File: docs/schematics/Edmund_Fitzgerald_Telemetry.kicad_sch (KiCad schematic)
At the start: 0 parts

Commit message: Save stable KiCAD schematic base with verified ESP32 pinout
- Verified all GPIO mappings against boat_telemetry.ino
- Established correct ESP32-WROOM-32 symbol and wiring base
- Includes labels for Audio, RC, Power, and Lighting sections
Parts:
- added U1: ESP32_Control, symbol MCU_Espressif:ESP32-WROOM-32
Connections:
- new net 3V3: U1.1 (3V3)
- new net BAT_SENSE: U1.5 (IO34)
- new net DFP_RX: U1.11 (IO27)
- new net DFP_TX: U1.10 (IO26)
- new net FLOOD_GATE: U1.33 (IO21)
- new net FLOOD_LED: U1.26 (IO4)
- new net GND: U1.15 (GND)
- new net I2S_BCLK: U1.9 (IO25)
- new net I2S_DIN: U1.37 (IO23)
- new net I2S_LRC: U1.36 (IO22)
- new net RUN_GATE: U1.25 (IO16)
- new net RUN_LED: U1.24 (IO2)
- new net SERVO_RC: U1.31 (IO19)
- new net THROTTLE_RC: U1.30 (IO18)
- new net WATER_SENSOR: U1.7 (IO32)
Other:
- removed sheet ?
- note added: "100k/47k Resistor Divider for 8.4V sensing"
- note added: "AUDIO SECTION"
- note added: "I2S: BCLK, LRC, DIN -> MAX98357A"
- note added: "IO16/IO21 drive N-Channel MOSFET Gates"
- note added: "LIGHTING SECTION"
- note added: "POWER SENSE"
- note added: "Throttle (IO18), Servo (IO19) 5V PWM"
- note added: "UART: TX, RX -> DFPlayer Pro"
- note removed: "AUDIO SYSTEM"
- note removed: "Battery ADC on GPIO 34 with voltage divider"
- note removed: "Built-in WiFi 2.4GHz for telemetry and OTA updates"
- note removed: "CAMERA SYSTEM"
- note removed: "CONNECTIVITY"
- note removed: "Connected to MAX98357A Class-D Amplifier"
- note removed: "Core 0 handles WiFi and HTTP Server"
- note removed: "Core 1 runs Audio Engine with real-time I2S"
- note removed: "DFPlayer Pro on GPIO 27 RX, 26 TX at 115200 baud"
- note removed: "GPIO 18 captures Throttle PWM signal"
- note removed: "GPIO 19 captures Servo Rudder PWM signal"
- note removed: "GPIO 2 and GPIO 16 control running lights"
- note removed: "GPIO 4 and GPIO 21 control flood lights"
- note removed: "I2S output on GPIO 25 (BCLK), 22 (LRC), 23 (DIN)"
- note removed: "LED CONTROL"
- note removed: "Main Controller: ESP32 Dual-Core"
- note removed: "POWER: 8.4V LiPo battery"
- note removed: "SENSORS"
- note removed: "Separate ESP32-CAM with AI-Thinker OV2640"
- note removed: "Water intrusion sensor on GPIO 32 with pullup"
- title: Edmund Fitzgerald Telemetry System -> Edmund Fitzgerald - Platform Telemetry
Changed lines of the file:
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@@
 (kicad_sch (version 20230121) (generator eeschema)
  (paper "A3")
- (title_block
-  (title "Edmund Fitzgerald Telemetry System")
-  (date "2026-01-31")
-  (rev "1.0")
-  (company "Project Edmund Fitzgerald")
- )
- (sheet (at 0 0) (size 297 210))
- (text "POWER: 8.4V LiPo battery"
-  (at 25 50 0)
-  (effects (font (size 2 2) (thickness 0.15)) (justify left))
- )
- (text "Main Controller: ESP32 Dual-Core"
-  (at 25 80 0)
-  (effects (font (size 1.5 1.5) (thickness 0.12)) (justify left))
- )
- (text "Core 0 handles WiFi and HTTP Server"
-  (at 25 95 0)
-  (effects (font (size 1 1) (thickness 0.1)) (justify left))
- )
- (text "Core 1 runs Audio Engine with real-time I2S"
-  (at 25 110 0)
-  (effects (font (size 1 1) (thickness 0.1)) (justify left))
- )
- (text "AUDIO SYSTEM"
-  (at 25 140 0)
-  (effects (font (size 1.5 1.5) (thickness 0.12)) (justify left))
- )
- (text "I2S output on GPIO 25 (BCLK), 22 (LRC), 23 (DIN)"
-  (at 25 155 0)
-  (effects (font (size 1 1) (thickness 0.1)) (justify left))
- )
- (text "Connected to MAX98357A Class-D Amplifier"
-  (at 25 170 0)
-  (effects (font (size 1 1) (thickness 0.1)) (justify left))
- )
- (text "DFPlayer Pro on GPIO 27 RX, 26 TX at 115200 baud"
-  (at 25 185 0)
-  (effects (font (size 1 1) (thickness 0.1)) (justify left))
- )
- (text "SENSORS"
-  (at 25 215 0)
-  (effects (font (size 1.5 1.5) (thickness 0.12)) (justify left))
- )
- (text "Battery ADC on GPIO 34 with voltage divider"
-  (at 25 230 0)
-  (effects (font (size 1 1) (thickness 0.1)) (justify left))
- )
- (text "Water intrusion sensor on GPIO 32 with pullup"
-  (at 25 245 0)
-  (effects (font (size 1 1) (thickness 0.1)) (justify left))
- )
- (text "LED CONTROL"
-  (at 25 275 0)
-  (effects (font (size 1.5 1.5) (thickness 0.12)) (justify left))
- )
- (text "GPIO 2 and GPIO 16 control running lights"
-  (at 25 290 0)
-  (effects (font (size 1 1) (thickness 0.1)) (justify left))
- )
- (text "GPIO 4 and GPIO 21 control flood lights"
-  (at 25 305 0)
-  (effects (font (size 1 1) (thickness 0.1)) (justify left))
- )
- (text "RC RECEIVER"
-  (at 25 335 0)
-  (effects (font (size 1.5 1.5) (thickness 0.12)) (justify left))
- )
- (text "GPIO 18 captures Throttle PWM signal"
-  (at 25 350 0)
-  (effects (font (size 1 1) (thickness 0.1)) (justify left))
- )
- (text "GPIO 19 captures Servo Rudder PWM signal"
-  (at 25 365 0)
-  (effects (font (size 1 1) (thickness 0.1)) (justify left))
- )
- (text "CAMERA SYSTEM"
-  (at 25 395 0)
-  (effects (font (size 1.5 1.5) (thickness 0.12)) (justify left))
- )
- (text "Separate ESP32-CAM with AI-Thinker OV2640"
-  (at 25 410 0)
-  (effects (font (size 1 1) (thickness 0.1)) (justify left))
- )
- (text "CONNECTIVITY"
-  (at 25 440 0)
-  (effects (font (size 1.5 1.5) (thickness 0.12)) (justify left))
- )
- (text "Built-in WiFi 2.4GHz for telemetry and OTA updates"
-  (at 25 455 0)
-  (effects (font (size 1 1) (thickness 0.1)) (justify left))
- )
+ (title_block (title "Edmund Fitzgerald - Platform Telemetry") (company "Project Edmund Fitzgerald") (rev "1.1") (date "2026-01-31"))
+ (symbol (lib_id "MCU_Espressif:ESP32-WROOM-32") (at 150 100 0) (unit 1) (in_bom yes) (on_board yes) (fields_autoplaced yes)
+  (property "Reference" "U1" (at 150 75 0)) (property "Value" "ESP32_Control" (at 150 125 0)))
+  (wire (pts (xy 134.76 84.76) (xy 120 84.76)) (stroke (width 0) (type solid)))
+  (label "3V3" (at 120 84.76 0) (effects (font (size 1.27 1.27)) (justify left bottom)))
+  (wire (pts (xy 134.76 94.92) (xy 120 94.92)) (stroke (width 0) (type solid)))
+  (label "BAT_SENSE" (at 120 94.92 0) (effects (font (size 1.27 1.27)) (justify left bottom)))
+  (wire (pts (xy 134.76 100) (xy 120 100)) (stroke (width 0) (type solid)))
+  (label "WATER_SENSOR" (at 120 100 0) (effects (font (size 1.27 1.27)) (justify left bottom)))
+  (wire (pts (xy 134.76 105.08) (xy 120 105.08)) (stroke (width 0) (type solid)))
+  (label "I2S_BCLK" (at 120 105.08 0) (effects (font (size 1.27 1.27)) (justify left bottom)))
+  (wire (pts (xy 134.76 107.62) (xy 120 107.62)) (stroke (width 0) (type solid)))
+  (label "DFP_TX" (at 120 107.62 0) (effects (font (size 1.27 1.27)) (justify left bottom)))
+  (wire (pts (xy 134.76 110.16) (xy 120 110.16)) (stroke (width 0) (type solid)))
+  (label "DFP_RX" (at 120 110.16 0) (effects (font (size 1.27 1.27)) (justify left bottom)))
+  (wire (pts (xy 150 120.32) (xy 150 130)) (stroke (width 0) (type solid)))
+  (label "GND" (at 150 130 90) (effects (font (size 1.27 1.27)) (justify left bottom)))
+  (wire (pts (xy 165.24 115.24) (xy 180 115.24)) (stroke (width 0) (type solid)))
+  (label "I2S_DIN" (at 180 115.24 0) (effects (font (size 1.27 1.27)) (justify left bottom)))
+  (wire (pts (xy 165.24 112.7) (xy 180 112.7)) (stroke (width 0) (type solid)))
+  (label "I2S_LRC" (at 180 112.7 0) (effects (font (size 1.27 1.27)) (justify left bottom)))
+  (wire (pts (xy 165.24 110.16) (xy 180 110.16)) (stroke (width 0) (type solid)))
+  (label "FLOOD_GATE" (at 180 110.16 0) (effects (font (size 1.27 1.27)) (justify left bottom)))
+  (wire (pts (xy 165.24 107.62) (xy 180 107.62)) (stroke (width 0) (type solid)))
+  (label "SERVO_RC" (at 180 107.62 0) (effects (font (size 1.27 1.27)) (justify left bottom)))
+  (wire (pts (xy 165.24 105.08) (xy 180 105.08)) (stroke (width 0) (type solid)))
+  (label "THROTTLE_RC" (at 180 105.08 0) (effects (font (size 1.27 1.27)) (justify left bottom)))
+  (wire (pts (xy 165.24 102.54) (xy 180 102.54)) (stroke (width 0) (type solid)))
+  (label "FLOOD_LED" (at 180 102.54 0) (effects (font (size 1.27 1.27)) (justify left bottom)))
+  (wire (pts (xy 165.24 100) (xy 180 100)) (stroke (width 0) (type solid)))
+  (label "RUN_LED" (at 180 100 0) (effects (font (size 1.27 1.27)) (justify left bottom)))
+  (wire (pts (xy 165.24 97.46) (xy 180 97.46)) (stroke (width 0) (type solid)))
+  (label "RUN_GATE" (at 180 97.46 0) (effects (font (size 1.27 1.27)) (justify left bottom)))
+ (text "AUDIO SECTION" (at 210 110 0) (effects (font (size 2 2)) (justify left)))
+ (text "I2S: BCLK, LRC, DIN -> MAX98357A" (at 210 118 0) (effects (font (size 1 1)) (justify left)))
+ (text "UART: TX, RX -> DFPlayer Pro" (at 210 123 0) (effects (font (size 1 1)) (justify left)))
+ (text "LIGHTING SECTION" (at 210 90 0) (effects (font (size 2 2)) (justify left)))
+ (text "IO16/IO21 drive N-Channel MOSFET Gates" (at 210 98 0) (effects (font (size 1 1)) (justify left)))
+ (text "RC RECEIVER" (at 210 140 0) (effects (font (size 2 2)) (justify left)))
+ (text "Throttle (IO18), Servo (IO19) 5V PWM" (at 210 148 0) (effects (font (size 1 1)) (justify left)))
+ (text "POWER SENSE" (at 80 90 0) (effects (font (size 2 2)) (justify right)))
+ (text "100k/47k Resistor Divider for 8.4V sensing" (at 80 98 0) (effects (font (size 1 1)) (justify right)))
 )

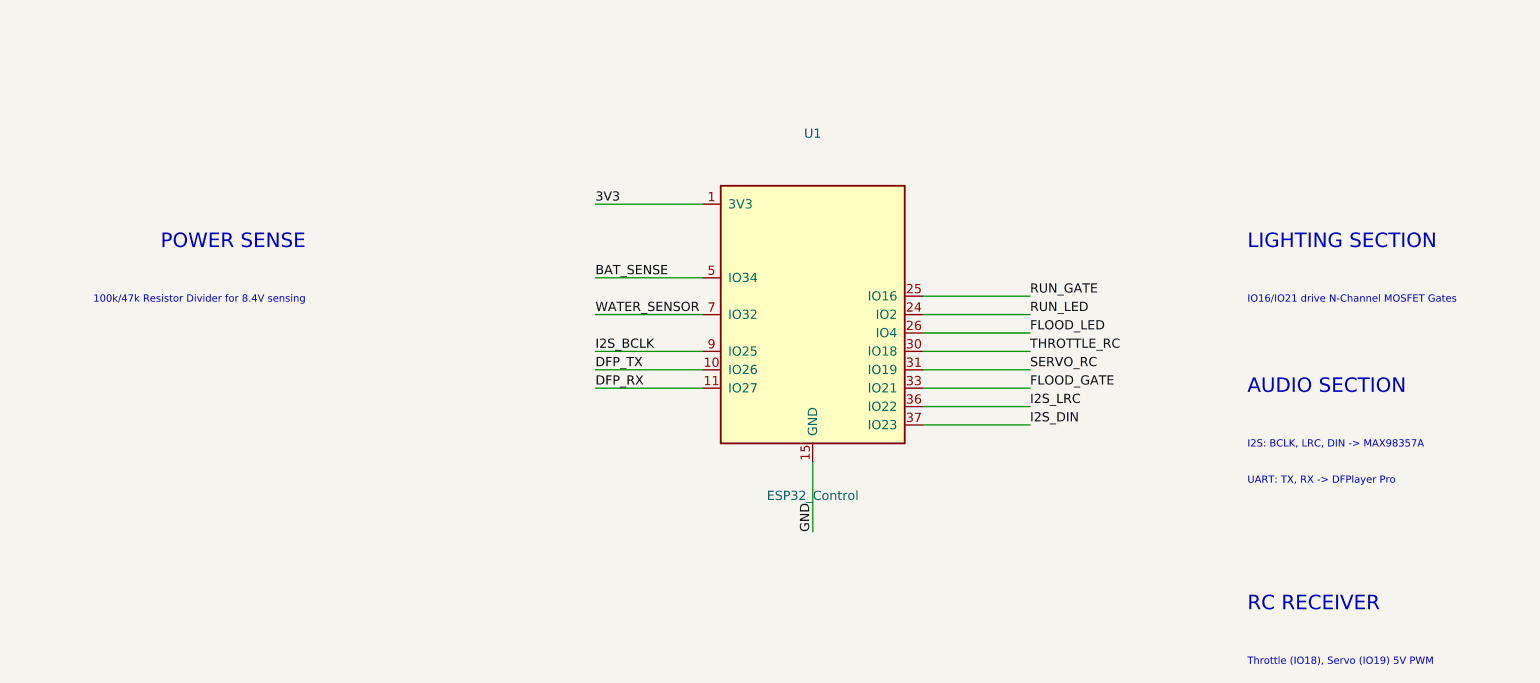
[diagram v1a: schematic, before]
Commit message: Add Running Light MOSFET circuit to schematic
- Integrated Q1 (N-MOSFET), R1 (Gate resistor), R2 (Pull-down)
- Added D1 (Running Light LED)
- Wired circuit to ESP32 IO16
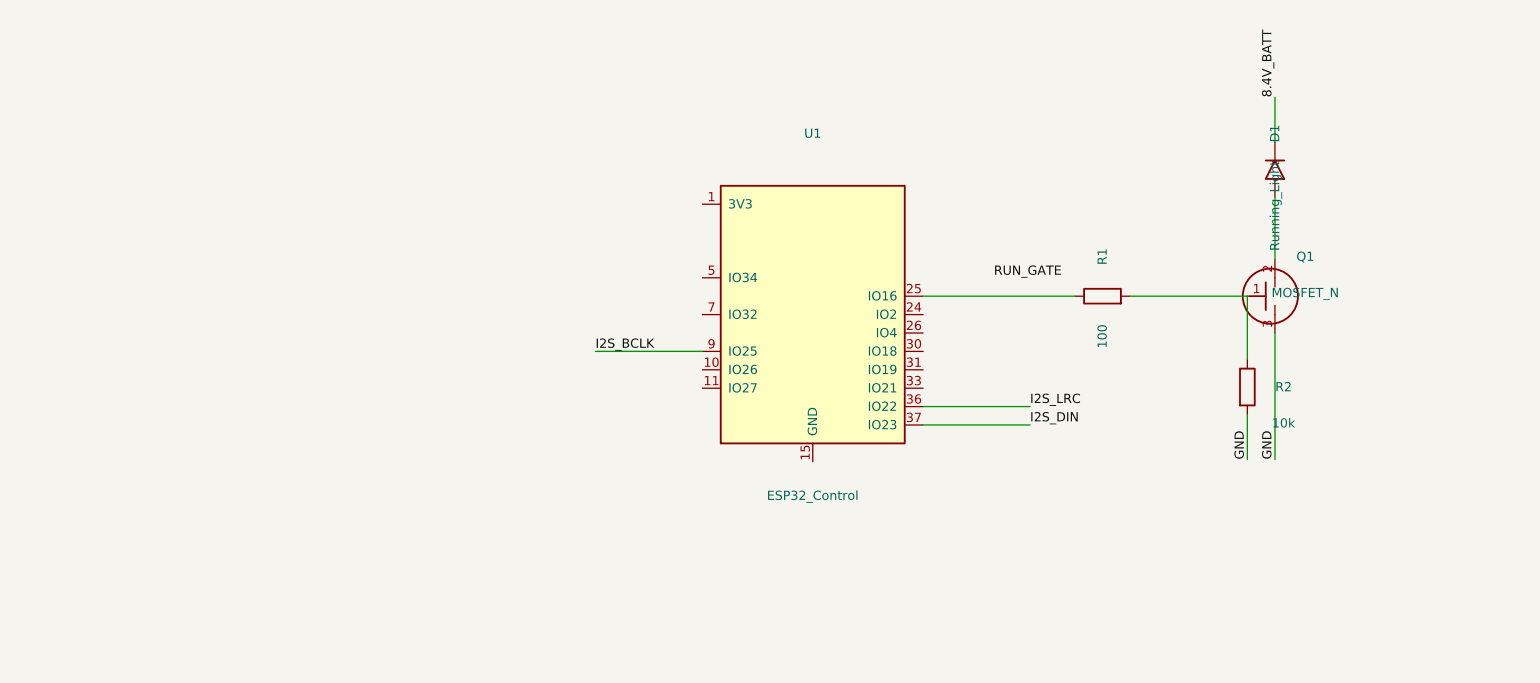
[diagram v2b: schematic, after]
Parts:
- added D1: Running_Light, symbol Device:LED
- added Q1: MOSFET_N, symbol Transistor_FET:Q_NMOS_GDS
- added R1: 100, symbol Device:R
- added R2: 10k, symbol Device:R
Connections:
- net GND: now also Q1.3 (S), R2.2; no longer U1.15 (GND)
- net RUN_GATE: no longer U1.25 (IO16)
- net 3V3: no longer names the net of U1.1 (3V3)
- net BAT_SENSE: no longer names the net of U1.5 (IO34)
- net DFP_RX: no longer names the net of U1.11 (IO27)
- net DFP_TX: no longer names the net of U1.10 (IO26)
- net FLOOD_GATE: no longer names the net of U1.33 (IO21)
- net FLOOD_LED: no longer names the net of U1.26 (IO4)
- net RUN_LED: no longer names the net of U1.24 (IO2)
- net SERVO_RC: no longer names the net of U1.31 (IO19)
- net THROTTLE_RC: no longer names the net of U1.30 (IO18)
- net WATER_SENSOR: no longer names the net of U1.7 (IO32)
- new net: Q1.1 (G), R1.2, R2.1
- new net: R1.1, U1.25 (IO16)
- new net: D1.1 (K), Q1.2 (D)
- new net 8.4V_BATT: D1.2 (A)
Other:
- note removed: "100k/47k Resistor Divider for 8.4V sensing"
- note removed: "AUDIO SECTION"
- note removed: "I2S: BCLK, LRC, DIN -> MAX98357A"
- note removed: "IO16/IO21 drive N-Channel MOSFET Gates"
- note removed: "LIGHTING SECTION"
- note removed: "POWER SENSE"
- note removed: "RC RECEIVER"
- note removed: "Throttle (IO18), Servo (IO19) 5V PWM"
- note removed: "UART: TX, RX -> DFPlayer Pro"
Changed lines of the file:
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@@
 (kicad_sch (version 20230121) (generator eeschema)
  (paper "A3")
- (title_block (title "Edmund Fitzgerald - Platform Telemetry") (company "Project Edmund Fitzgerald") (rev "1.1") (date "2026-01-31"))
+ (title_block (title "Edmund Fitzgerald - Platform Telemetry") (company "Project Edmund Fitzgerald") (rev "1.2") (date "2026-01-31"))
  (symbol (lib_id "MCU_Espressif:ESP32-WROOM-32") (at 150 100 0) (unit 1) (in_bom yes) (on_board yes) (fields_autoplaced yes)
   (property "Reference" "U1" (at 150 75 0)) (property "Value" "ESP32_Control" (at 150 125 0)))
-  (wire (pts (xy 134.76 84.76) (xy 120 84.76)) (stroke (width 0) (type solid)))
-  (label "3V3" (at 120 84.76 0) (effects (font (size 1.27 1.27)) (justify left bottom)))
-  (wire (pts (xy 134.76 94.92) (xy 120 94.92)) (stroke (width 0) (type solid)))
-  (label "BAT_SENSE" (at 120 94.92 0) (effects (font (size 1.27 1.27)) (justify left bottom)))
-  (wire (pts (xy 134.76 100) (xy 120 100)) (stroke (width 0) (type solid)))
-  (label "WATER_SENSOR" (at 120 100 0) (effects (font (size 1.27 1.27)) (justify left bottom)))
+ (symbol (lib_id "Device:R") (at 190 97.46 90) (unit 1) (in_bom yes) (on_board yes) (fields_autoplaced yes)
+  (property "Reference" "R1" (at 190 92 0)) (property "Value" "100" (at 190 103 0)))
+ (symbol (lib_id "Device:R") (at 210 110 0) (unit 1) (in_bom yes) (on_board yes) (fields_autoplaced yes)
+  (property "Reference" "R2" (at 215 110 0)) (property "Value" "10k" (at 215 115 0)))
+ (symbol (lib_id "Transistor_FET:Q_NMOS_GDS") (at 210 97.46 0) (unit 1) (in_bom yes) (on_board yes) (fields_autoplaced yes)
+  (property "Reference" "Q1" (at 218 92 0)) (property "Value" "MOSFET_N" (at 218 97 0)))
+ (symbol (lib_id "Device:LED") (at 213.81 80 90) (unit 1) (in_bom yes) (on_board yes) (fields_autoplaced yes)
+  (property "Reference" "D1" (at 213.81 75 0)) (property "Value" "Running_Light" (at 213.81 85 0)))
+  (wire (pts (xy 165.24 97.46) (xy 186.19 97.46)) (stroke (width 0) (type solid)))
+  (wire (pts (xy 193.81 97.46) (xy 210 97.46)) (stroke (width 0) (type solid)))
+  (wire (pts (xy 210 97.46) (xy 210 106.19)) (stroke (width 0) (type solid)))
+  (wire (pts (xy 210 113.81) (xy 210 120)) (stroke (width 0) (type solid)))
+  (wire (pts (xy 213.81 92.38) (xy 213.81 83.81)) (stroke (width 0) (type solid)))
+  (wire (pts (xy 213.81 76.19) (xy 213.81 70)) (stroke (width 0) (type solid)))
+  (wire (pts (xy 213.81 102.54) (xy 213.81 120)) (stroke (width 0) (type solid)))
+  (label "8.4V_BATT" (at 213.81 70 90) (effects (font (size 1.27 1.27)) (justify left bottom)))
+  (label "GND" (at 210 120 90) (effects (font (size 1.27 1.27)) (justify left bottom)))
+  (label "GND" (at 213.81 120 90) (effects (font (size 1.27 1.27)) (justify left bottom)))
+  (label "RUN_GATE" (at 175 95 0) (effects (font (size 1.27 1.27)) (justify left bottom)))
   (wire (pts (xy 134.76 105.08) (xy 120 105.08)) (stroke (width 0) (type solid)))
   (label "I2S_BCLK" (at 120 105.08 0) (effects (font (size 1.27 1.27)) (justify left bottom)))
-  (wire (pts (xy 134.76 107.62) (xy 120 107.62)) (stroke (width 0) (type solid)))
-  (label "DFP_TX" (at 120 107.62 0) (effects (font (size 1.27 1.27)) (justify left bottom)))
-  (wire (pts (xy 134.76 110.16) (xy 120 110.16)) (stroke (width 0) (type solid)))
-  (label "DFP_RX" (at 120 110.16 0) (effects (font (size 1.27 1.27)) (justify left bottom)))
-  (wire (pts (xy 150 120.32) (xy 150 130)) (stroke (width 0) (type solid)))
-  (label "GND" (at 150 130 90) (effects (font (size 1.27 1.27)) (justify left bottom)))
   (wire (pts (xy 165.24 115.24) (xy 180 115.24)) (stroke (width 0) (type solid)))
   (label "I2S_DIN" (at 180 115.24 0) (effects (font (size 1.27 1.27)) (justify left bottom)))
   (wire (pts (xy 165.24 112.7) (xy 180 112.7)) (stroke (width 0) (type solid)))
   (label "I2S_LRC" (at 180 112.7 0) (effects (font (size 1.27 1.27)) (justify left bottom)))
-  (wire (pts (xy 165.24 110.16) (xy 180 110.16)) (stroke (width 0) (type solid)))
-  (label "FLOOD_GATE" (at 180 110.16 0) (effects (font (size 1.27 1.27)) (justify left bottom)))
-  (wire (pts (xy 165.24 107.62) (xy 180 107.62)) (stroke (width 0) (type solid)))
-  (label "SERVO_RC" (at 180 107.62 0) (effects (font (size 1.27 1.27)) (justify left bottom)))
-  (wire (pts (xy 165.24 105.08) (xy 180 105.08)) (stroke (width 0) (type solid)))
-  (label "THROTTLE_RC" (at 180 105.08 0) (effects (font (size 1.27 1.27)) (justify left bottom)))
-  (wire (pts (xy 165.24 102.54) (xy 180 102.54)) (stroke (width 0) (type solid)))
-  (label "FLOOD_LED" (at 180 102.54 0) (effects (font (size 1.27 1.27)) (justify left bottom)))
-  (wire (pts (xy 165.24 100) (xy 180 100)) (stroke (width 0) (type solid)))
-  (label "RUN_LED" (at 180 100 0) (effects (font (size 1.27 1.27)) (justify left bottom)))
-  (wire (pts (xy 165.24 97.46) (xy 180 97.46)) (stroke (width 0) (type solid)))
-  (label "RUN_GATE" (at 180 97.46 0) (effects (font (size 1.27 1.27)) (justify left bottom)))
- (text "AUDIO SECTION" (at 210 110 0) (effects (font (size 2 2)) (justify left)))
- (text "I2S: BCLK, LRC, DIN -> MAX98357A" (at 210 118 0) (effects (font (size 1 1)) (justify left)))
- (text "UART: TX, RX -> DFPlayer Pro" (at 210 123 0) (effects (font (size 1 1)) (justify left)))
- (text "LIGHTING SECTION" (at 210 90 0) (effects (font (size 2 2)) (justify left)))
- (text "IO16/IO21 drive N-Channel MOSFET Gates" (at 210 98 0) (effects (font (size 1 1)) (justify left)))
- (text "RC RECEIVER" (at 210 140 0) (effects (font (size 2 2)) (justify left)))
- (text "Throttle (IO18), Servo (IO19) 5V PWM" (at 210 148 0) (effects (font (size 1 1)) (justify left)))
- (text "POWER SENSE" (at 80 90 0) (effects (font (size 2 2)) (justify right)))
- (text "100k/47k Resistor Divider for 8.4V sensing" (at 80 98 0) (effects (font (size 1 1)) (justify right)))
 )
